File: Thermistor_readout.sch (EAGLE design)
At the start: 22 parts, among them Q1 BC550C, U1 TI_NATIONAL_SEMICONDUCTOR_LF3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, U2 TI_NATIONAL_SEMICONDUCTOR_LF3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, U3 ANALOG_DEVICES_ADG725BSUZANAL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, U4 TI_NATIONAL_SEMICONDUCTOR_LF3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

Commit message: New_Re_size
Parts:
- RE: device 1AKarstenLib:R-EU_SMD0805H -> 1AKarstenLib:R-EU_SMD1206H
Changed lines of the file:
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@@
 <part name="R1" library="1AKarstenLib" deviceset="R-EU_SMD" device="0805H" value="1.1ΜΩ"/>
 <part name="R2" library="1AKarstenLib" deviceset="R-EU_SMD" device="0805H" value="1ΜΩ"/>
-<part name="RE" library="1AKarstenLib" deviceset="R-EU_SMD" device="0805H"/>
 <part name="R4" library="1AKarstenLib" deviceset="R-EU_SMD" device="0805H" value="1kΩ"/>
 <part name="Q1" library="transistor-npn" deviceset="BC550*" device="" technology="C"/>
@@
 <part name="P-2" library="supply1" deviceset="-15V" device=""/>
 <part name="GND14" library="supply1" deviceset="GND" device=""/>
+<part name="RE" library="1AKarstenLib" deviceset="R-EU_SMD" device="1206H"/>
 </parts>
 <sheets>
@@
 <instance part="R1" gate="G$1" x="35.56" y="99.06" rot="R90"/>
 <instance part="R2" gate="G$1" x="35.56" y="76.2" rot="R90"/>
-<instance part="RE" gate="G$1" x="53.34" y="71.12" rot="R90"/>
 <instance part="R4" gate="G$1" x="152.4" y="132.08"/>
 <instance part="Q1" gate="G$1" x="50.8" y="83.82"/>
@@
 <instance part="P-2" gate="1" x="132.08" y="66.04"/>
 <instance part="GND14" gate="1" x="152.4" y="71.12" rot="R90"/>
+<instance part="RE" gate="G$1" x="53.34" y="71.12" rot="R90"/>
 </instances>
 <busses>
@@
 <segment>
 <pinref part="Q1" gate="G$1" pin="E"/>
+<wire x1="53.34" y1="78.74" x2="53.34" y2="76.2" width="0.1524" layer="91"/>
 <pinref part="RE" gate="G$1" pin="2"/>
-<wire x1="53.34" y1="78.74" x2="53.34" y2="76.2" width="0.1524" layer="91"/>
 </segment>
 </net>
@@
 </segment>
 <segment>
-<pinref part="RE" gate="G$1" pin="1"/>
 <pinref part="GND3" gate="1" pin="GND"/>
 <wire x1="53.34" y1="66.04" x2="53.34" y2="63.5" width="0.1524" layer="91"/>
+<pinref part="RE" gate="G$1" pin="1"/>
 </segment>
 <segment>

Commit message: NewSchematicV1.1
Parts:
- added C10, C11, C9: (no value), 1AKarstenLib:C-EU_SMDC1206H/D
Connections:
- removed net -5V: CON2.26
- net +15V: now also C11.1, CON2.22; no longer CON2.20
- net +5V: now also C10.2, CON2.26; no longer CON2.24
- net -15V: now also C9.2, CON2.24; no longer CON2.22
- net GND: now also C10.1, C11.2, C9.1
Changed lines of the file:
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@@
 <part name="GND4" library="supply1" deviceset="GND" device=""/>
 <part name="P+1" library="supply1" deviceset="+5V" device=""/>
-<part name="P-1" library="supply1" deviceset="-5V" device=""/>
 <part name="P+2" library="supply1" deviceset="+5V" device=""/>
 <part name="P+4" library="supply1" deviceset="+5V" device=""/>
@@
 <part name="GND14" library="supply1" deviceset="GND" device=""/>
 <part name="RE" library="1AKarstenLib" deviceset="R-EU_SMD" device="1206H"/>
+<part name="GND15" library="supply1" deviceset="GND" device=""/>
+<part name="GND16" library="supply1" deviceset="GND" device=""/>
+<part name="GND17" library="supply1" deviceset="GND" device=""/>
+<part name="C9" library="1AKarstenLib" deviceset="C-EU_SMD" device="C1206H/D"/>
+<part name="C10" library="1AKarstenLib" deviceset="C-EU_SMD" device="C1206H/D"/>
+<part name="C11" library="1AKarstenLib" deviceset="C-EU_SMD" device="C1206H/D"/>
 </parts>
 <sheets>
@@
 <instance part="GND3" gate="1" x="53.34" y="60.96"/>
 <instance part="GND4" gate="1" x="172.72" y="58.42"/>
-<instance part="P+1" gate="1" x="152.4" y="30.48" rot="R90"/>
-<instance part="P-1" gate="1" x="152.4" y="33.02" rot="R270"/>
+<instance part="P+1" gate="1" x="170.18" y="33.02" rot="R90"/>
 <instance part="P+2" gate="1" x="35.56" y="152.4"/>
 <instance part="P+4" gate="1" x="66.04" y="38.1" rot="R90"/>
@@
 <instance part="GND11" gate="1" x="142.24" y="142.24" rot="R90"/>
 <instance part="GND12" gate="1" x="152.4" y="114.3" rot="R90"/>
-<instance part="P+7" gate="1" x="162.56" y="25.4" rot="R90"/>
-<instance part="P-4" gate="1" x="162.56" y="27.94" rot="R270"/>
+<instance part="P+7" gate="1" x="165.1" y="27.94" rot="R90"/>
+<instance part="P-4" gate="1" x="152.4" y="30.48" rot="R270"/>
 <instance part="P+9" gate="1" x="127" y="147.32"/>
 <instance part="P+10" gate="1" x="177.8" y="124.46"/>
@@
 <instance part="GND14" gate="1" x="152.4" y="71.12" rot="R90"/>
 <instance part="RE" gate="G$1" x="53.34" y="71.12" rot="R90"/>
+<instance part="GND15" gate="1" x="175.26" y="45.72" rot="R180"/>
+<instance part="GND16" gate="1" x="160.02" y="45.72" rot="R180"/>
+<instance part="GND17" gate="1" x="170.18" y="15.24"/>
+<instance part="C9" gate="G$1" x="160.02" y="38.1"/>
+<instance part="C10" gate="G$1" x="175.26" y="40.64"/>
+<instance part="C11" gate="G$1" x="170.18" y="25.4"/>
 </instances>
 <busses>
@@
 <wire x1="149.86" y1="71.12" x2="147.32" y2="71.12" width="0.1524" layer="91"/>
 </segment>
+<segment>
+<pinref part="GND16" gate="1" pin="GND"/>
+<pinref part="C9" gate="G$1" pin="1"/>
+<wire x1="160.02" y1="40.64" x2="160.02" y2="43.18" width="0.1524" layer="91"/>
+</segment>
+<segment>
+<pinref part="GND15" gate="1" pin="GND"/>
+<pinref part="C10" gate="G$1" pin="1"/>
+</segment>
+<segment>
+<pinref part="GND17" gate="1" pin="GND"/>
+<pinref part="C11" gate="G$1" pin="2"/>
+<wire x1="170.18" y1="17.78" x2="170.18" y2="20.32" width="0.1524" layer="91"/>
+</segment>
 </net>
 <net name="+5V" class="0">
@@
 </segment>
 <segment>
-<pinref part="P+1" gate="1" pin="+5V"/>
-<pinref part="CON2" gate="A" pin="24"/>
-<wire x1="154.94" y1="30.48" x2="177.8" y2="30.48" width="0.1524" layer="91"/>
-</segment>
-<segment>
 <pinref part="P+4" gate="1" pin="+5V"/>
 <pinref part="U3" gate="G$0" pin="1_VDD"/>
@@
 <junction x="86.36" y="22.86"/>
 </segment>
-</net>
-<net name="-5V" class="0">
-<segment>
-<pinref part="P-1" gate="1" pin="-5V"/>
+<segment>
+<pinref part="P+1" gate="1" pin="+5V"/>
 <pinref part="CON2" gate="A" pin="26"/>
-<wire x1="154.94" y1="33.02" x2="177.8" y2="33.02" width="0.1524" layer="91"/>
+<wire x1="172.72" y1="33.02" x2="175.26" y2="33.02" width="0.1524" layer="91"/>
+<pinref part="C10" gate="G$1" pin="2"/>
+<wire x1="175.26" y1="33.02" x2="177.8" y2="33.02" width="0.1524" layer="91"/>
+<wire x1="175.26" y1="33.02" x2="175.26" y2="35.56" width="0.1524" layer="91"/>
+<junction x="175.26" y="33.02"/>
 </segment>
 </net>
@@
 </segment>
 <segment>
-<pinref part="P+7" gate="1" pin="+15V"/>
-<pinref part="CON2" gate="A" pin="20"/>
-<wire x1="165.1" y1="25.4" x2="177.8" y2="25.4" width="0.1524" layer="91"/>
-</segment>
-<segment>
 <pinref part="U2" gate="G$0" pin="V+"/>
 <wire x1="177.8" y1="121.92" x2="177.8" y2="119.38" width="0.1524" layer="91"/>
@@
 <wire x1="127" y1="93.98" x2="132.08" y2="93.98" width="0.1524" layer="91"/>
 </segment>
+<segment>
+<pinref part="P+7" gate="1" pin="+15V"/>
+<pinref part="CON2" gate="A" pin="22"/>
+<wire x1="167.64" y1="27.94" x2="170.18" y2="27.94" width="0.1524" layer="91"/>
+<pinref part="C11" gate="G$1" pin="1"/>
+<wire x1="170.18" y1="27.94" x2="177.8" y2="27.94" width="0.1524" layer="91"/>
+<junction x="170.18" y="27.94"/>
+</segment>
 </net>
 <net name="-15V" class="0">
@@
 </segment>
 <segment>
-<pinref part="P-4" gate="1" pin="-15V"/>
-<pinref part="CON2" gate="A" pin="22"/>
-<wire x1="165.1" y1="27.94" x2="177.8" y2="27.94" width="0.1524" layer="91"/>
-</segment>
-<segment>
 <pinref part="U2" gate="G$0" pin="V-"/>
 <wire x1="177.8" y1="86.36" x2="177.8" y2="88.9" width="0.1524" layer="91"/>
@@
 <pinref part="P-2" gate="1" pin="-15V"/>
 </segment>
-</net>
+<segment>
+<pinref part="P-4" gate="1" pin="-15V"/>
+<pinref part="CON2" gate="A" pin="24"/>
+<wire x1="154.94" y1="30.48" x2="160.02" y2="30.48" width="0.1524" layer="91"/>
+<pinref part="C9" gate="G$1" pin="2"/>
+<wire x1="160.02" y1="30.48" x2="177.8" y2="30.48" width="0.1524" layer="91"/>
+<wire x1="160.02" y1="30.48" x2="160.02" y2="33.02" width="0.1524" layer="91"/>
+<junction x="160.02" y="30.48"/>
+</segment>
+</net>

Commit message: Internal_switch_v1.1
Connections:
- net +5V: now also CON2.1; no longer CON2.26
- net -15V: now also CON2.26; no longer CON2.24
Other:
- moved on the sheet: C10, C9
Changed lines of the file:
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@@
 <instance part="GND3" gate="1" x="53.34" y="60.96"/>
 <instance part="GND4" gate="1" x="172.72" y="58.42"/>
-<instance part="P+1" gate="1" x="170.18" y="33.02" rot="R90"/>
+<instance part="P+1" gate="1" x="213.36" y="2.54" rot="R270"/>
 <instance part="P+2" gate="1" x="35.56" y="152.4"/>
 <instance part="P+4" gate="1" x="66.04" y="38.1" rot="R90"/>
@@
 <instance part="GND12" gate="1" x="152.4" y="114.3" rot="R90"/>
 <instance part="P+7" gate="1" x="165.1" y="27.94" rot="R90"/>
-<instance part="P-4" gate="1" x="152.4" y="30.48" rot="R270"/>
+<instance part="P-4" gate="1" x="154.94" y="33.02" rot="R270"/>
 <instance part="P+9" gate="1" x="127" y="147.32"/>
 <instance part="P+10" gate="1" x="177.8" y="124.46"/>
@@
 <instance part="GND14" gate="1" x="152.4" y="71.12" rot="R90"/>
 <instance part="RE" gate="G$1" x="53.34" y="71.12" rot="R90"/>
-<instance part="GND15" gate="1" x="175.26" y="45.72" rot="R180"/>
-<instance part="GND16" gate="1" x="160.02" y="45.72" rot="R180"/>
+<instance part="GND15" gate="1" x="200.66" y="17.78" rot="R180"/>
+<instance part="GND16" gate="1" x="160.02" y="50.8" rot="R180"/>
 <instance part="GND17" gate="1" x="170.18" y="15.24"/>
-<instance part="C9" gate="G$1" x="160.02" y="38.1"/>
-<instance part="C10" gate="G$1" x="175.26" y="40.64"/>
+<instance part="C9" gate="G$1" x="160.02" y="43.18"/>
+<instance part="C10" gate="G$1" x="200.66" y="10.16"/>
 <instance part="C11" gate="G$1" x="170.18" y="25.4"/>
 </instances>
@@
 <pinref part="GND16" gate="1" pin="GND"/>
 <pinref part="C9" gate="G$1" pin="1"/>
-<wire x1="160.02" y1="40.64" x2="160.02" y2="43.18" width="0.1524" layer="91"/>
+<wire x1="160.02" y1="45.72" x2="160.02" y2="48.26" width="0.1524" layer="91"/>
 </segment>
 <segment>
 <pinref part="GND15" gate="1" pin="GND"/>
 <pinref part="C10" gate="G$1" pin="1"/>
+<wire x1="200.66" y1="15.24" x2="200.66" y2="12.7" width="0.1524" layer="91"/>
 </segment>
 <segment>
@@
 </segment>
 <segment>
+<pinref part="CON2" gate="A" pin="1"/>
 <pinref part="P+1" gate="1" pin="+5V"/>
-<pinref part="CON2" gate="A" pin="26"/>
-<wire x1="172.72" y1="33.02" x2="175.26" y2="33.02" width="0.1524" layer="91"/>
+<wire x1="193.04" y1="2.54" x2="200.66" y2="2.54" width="0.1524" layer="91"/>
 <pinref part="C10" gate="G$1" pin="2"/>
-<wire x1="175.26" y1="33.02" x2="177.8" y2="33.02" width="0.1524" layer="91"/>
-<wire x1="175.26" y1="33.02" x2="175.26" y2="35.56" width="0.1524" layer="91"/>
-<junction x="175.26" y="33.02"/>
+<wire x1="200.66" y1="2.54" x2="210.82" y2="2.54" width="0.1524" layer="91"/>
+<wire x1="200.66" y1="2.54" x2="200.66" y2="5.08" width="0.1524" layer="91"/>
+<junction x="200.66" y="2.54"/>
 </segment>
 </net>
@@
 </segment>
 <segment>
+<pinref part="CON2" gate="A" pin="26"/>
 <pinref part="P-4" gate="1" pin="-15V"/>
-<pinref part="CON2" gate="A" pin="24"/>
-<wire x1="154.94" y1="30.48" x2="160.02" y2="30.48" width="0.1524" layer="91"/>
+<wire x1="157.48" y1="33.02" x2="160.02" y2="33.02" width="0.1524" layer="91"/>
 <pinref part="C9" gate="G$1" pin="2"/>
-<wire x1="160.02" y1="30.48" x2="177.8" y2="30.48" width="0.1524" layer="91"/>
-<wire x1="160.02" y1="30.48" x2="160.02" y2="33.02" width="0.1524" layer="91"/>
-<junction x="160.02" y="30.48"/>
-</segment>
-</net>
+<wire x1="160.02" y1="33.02" x2="177.8" y2="33.02" width="0.1524" layer="91"/>
+<wire x1="160.02" y1="38.1" x2="160.02" y2="33.02" width="0.1524" layer="91"/>
+<junction x="160.02" y="33.02"/>
+</segment>
+</net>

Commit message: new_connector
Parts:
- removed CON2: (no value), con-harting:CON26L
- added CON1: (no value), con-harting:CON16L
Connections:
- net +15V: now also CON1.12; no longer CON2.22
- net +5V: now also CON1.1; no longer CON2.1
- net -15V: now also CON1.16; no longer CON2.26
- net GND: now also CON1.15; no longer CON2.25
- net N$11: now also CON1.6; no longer CON2.6
- net N$13: now also CON1.2; no longer CON2.2
- net N$14: now also CON1.4; no longer CON2.4
- net N$24: now also CON1.8; no longer CON2.8
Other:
- moved on the sheet: C10, C11
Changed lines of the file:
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@@
 <part name="C3" library="1AKarstenLib" deviceset="C-EU_SMD" device="R0805H"/>
 <part name="C4" library="1AKarstenLib" deviceset="C-EU_SMD" device="R0805H"/>
-<part name="CON2" library="con-harting" deviceset="CON26L" device=""/>
 <part name="GND5" library="supply1" deviceset="GND" device=""/>
 <part name="GND8" library="supply1" deviceset="GND" device=""/>
@@
 <part name="C10" library="1AKarstenLib" deviceset="C-EU_SMD" device="C1206H/D"/>
 <part name="C11" library="1AKarstenLib" deviceset="C-EU_SMD" device="C1206H/D"/>
+<part name="CON1" library="con-harting" deviceset="CON16L" device=""/>
 </parts>
 <sheets>
@@
 <instance part="GND3" gate="1" x="53.34" y="60.96"/>
 <instance part="GND4" gate="1" x="172.72" y="58.42"/>
-<instance part="P+1" gate="1" x="213.36" y="2.54" rot="R270"/>
+<instance part="P+1" gate="1" x="213.36" y="15.24" rot="R270"/>
 <instance part="P+2" gate="1" x="35.56" y="152.4"/>
 <instance part="P+4" gate="1" x="66.04" y="38.1" rot="R90"/>
@@
 <instance part="C3" gate="G$1" x="190.5" y="88.9" rot="R270"/>
 <instance part="C4" gate="G$1" x="182.88" y="119.38" rot="R90"/>
-<instance part="CON2" gate="A" x="185.42" y="17.78"/>
 <instance part="GND5" gate="1" x="193.04" y="119.38" rot="R90"/>
 <instance part="GND8" gate="1" x="198.12" y="88.9" rot="R90"/>
@@
 <instance part="GND11" gate="1" x="142.24" y="142.24" rot="R90"/>
 <instance part="GND12" gate="1" x="152.4" y="114.3" rot="R90"/>
-<instance part="P+7" gate="1" x="165.1" y="27.94" rot="R90"/>
+<instance part="P+7" gate="1" x="154.94" y="27.94" rot="R90"/>
 <instance part="P-4" gate="1" x="154.94" y="33.02" rot="R270"/>
 <instance part="P+9" gate="1" x="127" y="147.32"/>
@@
 <instance part="GND14" gate="1" x="152.4" y="71.12" rot="R90"/>
 <instance part="RE" gate="G$1" x="53.34" y="71.12" rot="R90"/>
-<instance part="GND15" gate="1" x="200.66" y="17.78" rot="R180"/>
+<instance part="GND15" gate="1" x="205.74" y="30.48" rot="R180"/>
 <instance part="GND16" gate="1" x="160.02" y="50.8" rot="R180"/>
-<instance part="GND17" gate="1" x="170.18" y="15.24"/>
+<instance part="GND17" gate="1" x="162.56" y="15.24"/>
 <instance part="C9" gate="G$1" x="160.02" y="43.18"/>
-<instance part="C10" gate="G$1" x="200.66" y="10.16"/>
-<instance part="C11" gate="G$1" x="170.18" y="25.4"/>
+<instance part="C10" gate="G$1" x="205.74" y="22.86"/>
+<instance part="C11" gate="G$1" x="162.56" y="25.4"/>
+<instance part="CON1" gate="G$1" x="185.42" y="25.4"/>
 </instances>
 <busses>
@@
 <wire x1="187.96" y1="104.14" x2="210.82" y2="104.14" width="0.1524" layer="91"/>
 <wire x1="210.82" y1="104.14" x2="210.82" y2="48.26" width="0.1524" layer="91"/>
-<pinref part="CON2" gate="A" pin="8"/>
-<wire x1="177.8" y1="10.16" x2="149.86" y2="10.16" width="0.1524" layer="91"/>
+<wire x1="167.64" y1="10.16" x2="149.86" y2="10.16" width="0.1524" layer="91"/>
 <wire x1="149.86" y1="10.16" x2="149.86" y2="48.26" width="0.1524" layer="91"/>
 <wire x1="149.86" y1="48.26" x2="210.82" y2="48.26" width="0.1524" layer="91"/>
@@
 <wire x1="210.82" y1="132.08" x2="210.82" y2="104.14" width="0.1524" layer="91"/>
 <junction x="210.82" y="104.14"/>
+<wire x1="167.64" y1="10.16" x2="167.64" y2="22.86" width="0.1524" layer="91"/>
+<pinref part="CON1" gate="G$1" pin="8"/>
+<wire x1="167.64" y1="22.86" x2="177.8" y2="22.86" width="0.1524" layer="91"/>
 </segment>
 </net>
@@
 </segment>
 <segment>
-<pinref part="CON2" gate="A" pin="25"/>
 <pinref part="GND1" gate="1" pin="GND"/>
-<wire x1="195.58" y1="33.02" x2="193.04" y2="33.02" width="0.1524" layer="91"/>
+<pinref part="CON1" gate="G$1" pin="15"/>
+<wire x1="193.04" y1="33.02" x2="195.58" y2="33.02" width="0.1524" layer="91"/>
 </segment>
 <segment>
@@
 <pinref part="GND15" gate="1" pin="GND"/>
 <pinref part="C10" gate="G$1" pin="1"/>
-<wire x1="200.66" y1="15.24" x2="200.66" y2="12.7" width="0.1524" layer="91"/>
+<wire x1="205.74" y1="27.94" x2="205.74" y2="25.4" width="0.1524" layer="91"/>
 </segment>
 <segment>
 <pinref part="GND17" gate="1" pin="GND"/>
 <pinref part="C11" gate="G$1" pin="2"/>
-<wire x1="170.18" y1="17.78" x2="170.18" y2="20.32" width="0.1524" layer="91"/>
+<wire x1="162.56" y1="17.78" x2="162.56" y2="20.32" width="0.1524" layer="91"/>
 </segment>
 </net>
@@
 </segment>
 <segment>
-<pinref part="CON2" gate="A" pin="1"/>
 <pinref part="P+1" gate="1" pin="+5V"/>
-<wire x1="193.04" y1="2.54" x2="200.66" y2="2.54" width="0.1524" layer="91"/>
 <pinref part="C10" gate="G$1" pin="2"/>
-<wire x1="200.66" y1="2.54" x2="210.82" y2="2.54" width="0.1524" layer="91"/>
-<wire x1="200.66" y1="2.54" x2="200.66" y2="5.08" width="0.1524" layer="91"/>
-<junction x="200.66" y="2.54"/>
+<wire x1="205.74" y1="15.24" x2="210.82" y2="15.24" width="0.1524" layer="91"/>
+<wire x1="205.74" y1="15.24" x2="205.74" y2="17.78" width="0.1524" layer="91"/>
+<pinref part="CON1" gate="G$1" pin="1"/>
+<wire x1="205.74" y1="15.24" x2="193.04" y2="15.24" width="0.1524" layer="91"/>
+<junction x="205.74" y="15.24"/>
 </segment>
 </net>
@@
 <wire x1="116.84" y1="43.18" x2="142.24" y2="43.18" width="0.1524" layer="91"/>
 <wire x1="142.24" y1="43.18" x2="142.24" y2="2.54" width="0.1524" layer="91"/>
-<pinref part="CON2" gate="A" pin="2"/>
-<wire x1="142.24" y1="2.54" x2="177.8" y2="2.54" width="0.1524" layer="91"/>
+<wire x1="142.24" y1="2.54" x2="175.26" y2="2.54" width="0.1524" layer="91"/>
+<wire x1="175.26" y1="2.54" x2="175.26" y2="15.24" width="0.1524" layer="91"/>
+<pinref part="CON1" gate="G$1" pin="2"/>
+<wire x1="175.26" y1="15.24" x2="177.8" y2="15.24" width="0.1524" layer="91"/>
 </segment>
 </net>
@@
 <wire x1="116.84" y1="45.72" x2="144.78" y2="45.72" width="0.1524" layer="91"/>
 <wire x1="144.78" y1="45.72" x2="144.78" y2="5.08" width="0.1524" layer="91"/>
-<pinref part="CON2" gate="A" pin="4"/>
-<wire x1="144.78" y1="5.08" x2="177.8" y2="5.08" width="0.1524" layer="91"/>
+<wire x1="144.78" y1="5.08" x2="172.72" y2="5.08" width="0.1524" layer="91"/>
+<wire x1="172.72" y1="5.08" x2="172.72" y2="17.78" width="0.1524" layer="91"/>
+<pinref part="CON1" gate="G$1" pin="4"/>
+<wire x1="172.72" y1="17.78" x2="177.8" y2="17.78" width="0.1524" layer="91"/>
 </segment>
 </net>
@@
 <wire x1="116.84" y1="48.26" x2="147.32" y2="48.26" width="0.1524" layer="91"/>
 <wire x1="147.32" y1="48.26" x2="147.32" y2="7.62" width="0.1524" layer="91"/>
-<pinref part="CON2" gate="A" pin="6"/>
-<wire x1="147.32" y1="7.62" x2="177.8" y2="7.62" width="0.1524" layer="91"/>
+<wire x1="147.32" y1="7.62" x2="170.18" y2="7.62" width="0.1524" layer="91"/>
+<wire x1="170.18" y1="7.62" x2="170.18" y2="20.32" width="0.1524" layer="91"/>
+<pinref part="CON1" gate="G$1" pin="6"/>
+<wire x1="170.18" y1="20.32" x2="177.8" y2="20.32" width="0.1524" layer="91"/>
 </segment>
 </net>
@@
 <segment>
 <pinref part="P+7" gate="1" pin="+15V"/>
-<pinref part="CON2" gate="A" pin="22"/>
-<wire x1="167.64" y1="27.94" x2="170.18" y2="27.94" width="0.1524" layer="91"/>
+<wire x1="157.48" y1="27.94" x2="162.56" y2="27.94" width="0.1524" layer="91"/>
 <pinref part="C11" gate="G$1" pin="1"/>
-<wire x1="170.18" y1="27.94" x2="177.8" y2="27.94" width="0.1524" layer="91"/>
-<junction x="170.18" y="27.94"/>
+<wire x1="162.56" y1="27.94" x2="177.8" y2="27.94" width="0.1524" layer="91"/>
+<junction x="162.56" y="27.94"/>
+<pinref part="CON1" gate="G$1" pin="12"/>
 </segment>
 </net>
@@
 </segment>
 <segment>
-<pinref part="CON2" gate="A" pin="26"/>
 <pinref part="P-4" gate="1" pin="-15V"/>
 <wire x1="157.48" y1="33.02" x2="160.02" y2="33.02" width="0.1524" layer="91"/>
@@
 <wire x1="160.02" y1="38.1" x2="160.02" y2="33.02" width="0.1524" layer="91"/>
 <junction x="160.02" y="33.02"/>
-</segment>
-</net>
+<pinref part="CON1" gate="G$1" pin="16"/>
+</segment>
+</net>

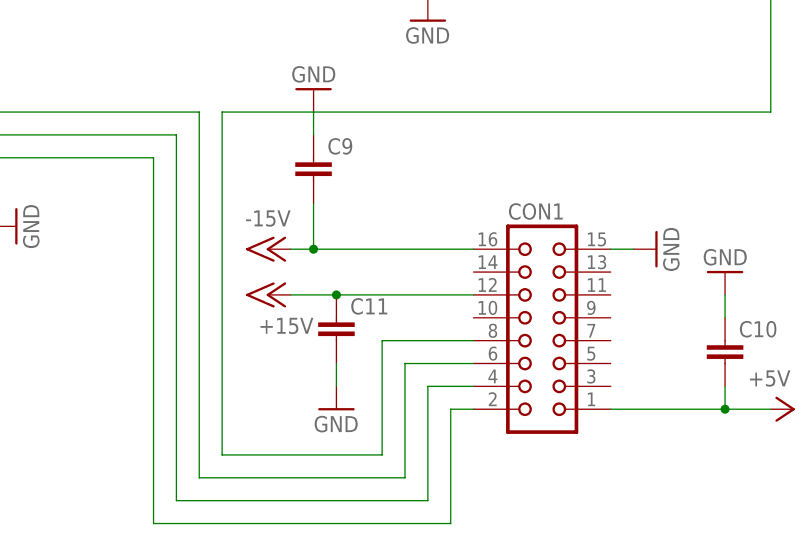
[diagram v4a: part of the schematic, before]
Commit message: Updated_Flat_cable_connections
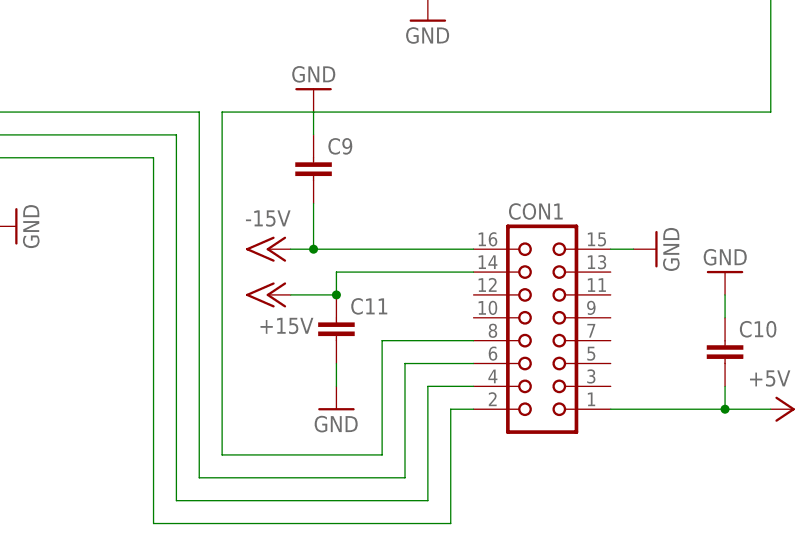
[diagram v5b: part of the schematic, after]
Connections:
- net +15V: now also CON1.14; no longer CON1.12
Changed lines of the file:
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@@
 <wire x1="157.48" y1="27.94" x2="162.56" y2="27.94" width="0.1524" layer="91"/>
 <pinref part="C11" gate="G$1" pin="1"/>
-<wire x1="162.56" y1="27.94" x2="177.8" y2="27.94" width="0.1524" layer="91"/>
+<wire x1="162.56" y1="27.94" x2="162.56" y2="30.48" width="0.1524" layer="91"/>
 <junction x="162.56" y="27.94"/>
-<pinref part="CON1" gate="G$1" pin="12"/>
+<pinref part="CON1" gate="G$1" pin="14"/>
+<wire x1="162.56" y1="30.48" x2="177.8" y2="30.48" width="0.1524" layer="91"/>
 </segment>
 </net>
